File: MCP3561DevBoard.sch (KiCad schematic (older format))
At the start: 51 parts, among them J1 Conn_Coaxial, J2 Conn_Coaxial, J3 Conn_02x03_Counter_Clockwise, J4 Conn_02x03_Counter_Clockwise, J5 Conn_01x04, J6 Conn_02x03_Counter_Clockwise, J7 Conn_01x10_Male, J8 Screw_Terminal_01x02, U3 TLV9051, U4 ADR366, U5 ADP3330-X, U6 ADP3330-X, U7 MCP3561, U8 Teensy4.1

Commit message: fixed power plane so that it contains voltage reference
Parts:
- added TP9: EXT_SYNC, my_library_foot:TestPoint_Keystone_5000-5004_Miniature, symbol Connector:TestPoint
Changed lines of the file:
@@
 Wire Wire Line
 	1350 6800 1900 6800
-Wire Wire Line
-	1900 7150 2300 7150
 Connection ~ 1900 7150
 Wire Wire Line
@@
 Wire Wire Line
 	1350 5150 1150 5150
+$Comp
+L Connector:TestPoint TP9
+U 1 1 604E5F5B
+P 2450 7150
+F 0 "TP9" H 2508 7268 50  0000 L CNN
+F 1 "EXT_SYNC" H 2508 7177 50  0000 L CNN
+F 2 "my_library_foot:TestPoint_Keystone_5000-5004_Miniature" H 2650 7150 50  0001 C CNN
+F 3 "~" H 2650 7150 50  0001 C CNN
+	1    2450 7150
+	1    0    0    -1
+$EndComp
+Wire Wire Line
+	1900 7150 2450 7150
 $EndSCHEMATC

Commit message: updated schematic and backup
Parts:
- R12: value R_US -> 10R
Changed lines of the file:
@@
 P 7150 4500
 F 0 "R12" H 7218 4546 50  0000 L CNN
-F 1 "R_US" H 7218 4455 50  0000 L CNN
+F 1 "10R" H 7218 4455 50  0000 L CNN
 F 2 "Resistor_SMD:R_0805_2012Metric_Pad1.15x1.40mm_HandSolder" V 7190 4490 50  0001 C CNN
 F 3 "~" H 7150 4500 50  0001 C CNN

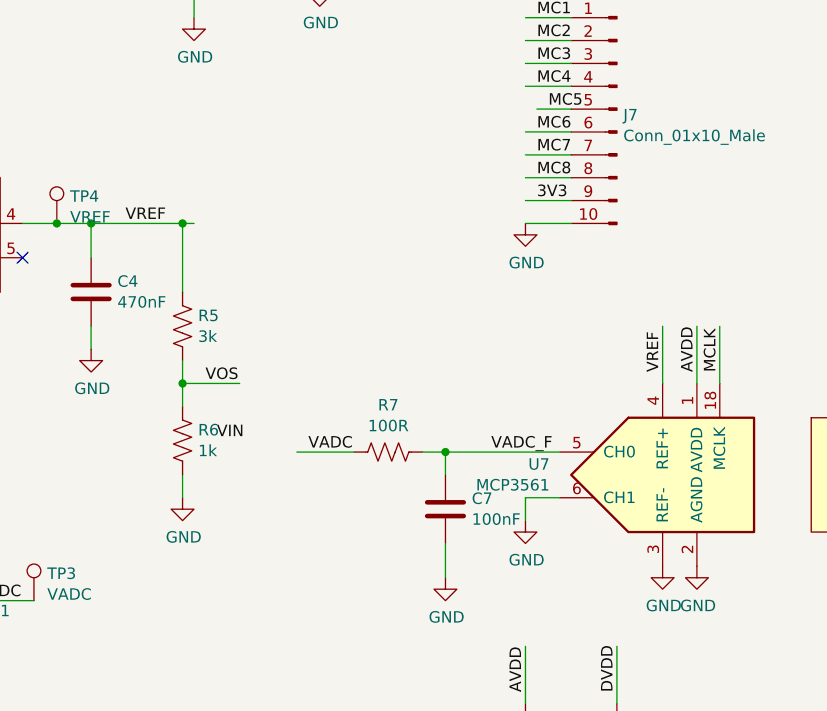
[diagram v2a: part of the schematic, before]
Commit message: added basic arduino code for SCPI communication over serial with arduino. Tested and works at 4.8kHz, there is some funky stuff going on at 38kHz, the ADC has a lower resolution and I'm not sure how to get around that
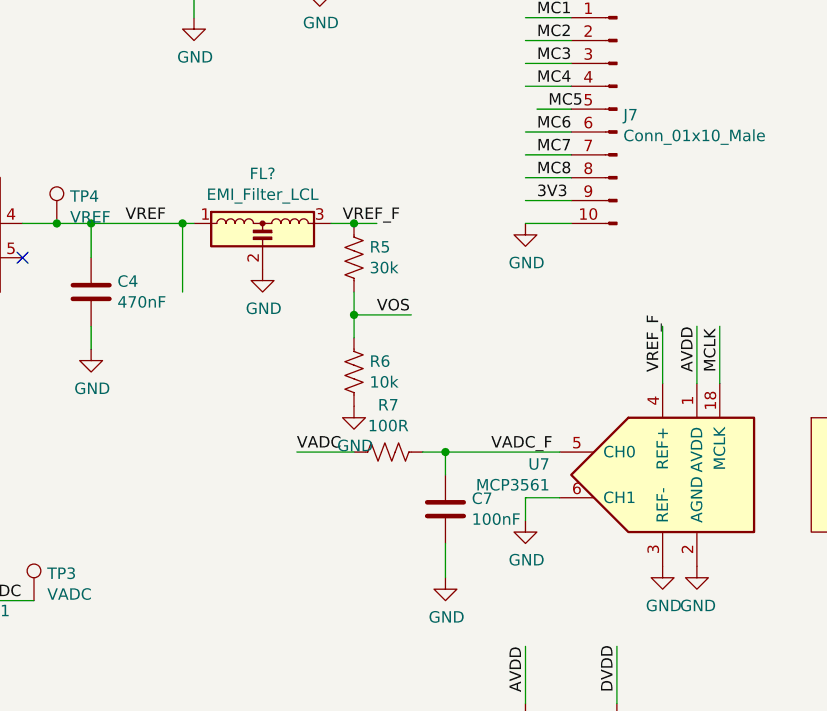
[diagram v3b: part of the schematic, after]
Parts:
- added FL?: EMI_Filter_LCL, my_library_foot:0805_3TERM, symbol Device:EMI_Filter_LCL
- R5: value 3k -> 30k
- R6: value 1k -> 10k
- U3: footprint Package_TO_SOT_SMD:SOT-353_SC-70-5 -> Package_TO_SOT_SMD:SOT-23-5_HandSoldering
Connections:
- net labels added: VREF_F
- wire segments 153 -> 154
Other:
- moved on the sheet: R5, R6
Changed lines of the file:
@@
 Wire Wire Line
 	1100 6300 1100 6150
-Text Label 4200 5150 0    50   ~ 0
-VIN
 $Comp
 L power:GND #PWR029
@@
 	6150 4900 6150 4650
 Text Label 6150 4850 1    50   ~ 0
-VREF
+VREF_F
 Wire Wire Line
 	6400 4900 6400 4650
@@
 F 0 "U3" H 2994 5896 50  0000 L CNN
 F 1 "TLV9051" H 2994 5805 50  0000 L CNN
-F 2 "Package_TO_SOT_SMD:SOT-353_SC-70-5" H 2750 5850 50  0001 C CNN
+F 2 "Package_TO_SOT_SMD:SOT-23-5_HandSoldering" H 2750 5850 50  0001 C CNN
 F 3 "http://www.ti.com/lit/ds/symlink/tlv172.pdf" H 2550 5850 50  0001 C CNN
 	1    2550 5850
@@
 L Device:R_US R5
 U 1 1 600653AE
-P 4050 4650
-F 0 "R5" H 4118 4696 50  0000 L CNN
-F 1 "3k" H 4118 4605 50  0000 L CNN
-F 2 "Resistor_SMD:R_0805_2012Metric_Pad1.15x1.40mm_HandSolder" V 4090 4640 50  0001 C CNN
-F 3 "~" H 4050 4650 50  0001 C CNN
-	1    4050 4650
+P 4800 4350
+F 0 "R5" H 4868 4396 50  0000 L CNN
+F 1 "30k" H 4868 4305 50  0000 L CNN
+F 2 "Resistor_SMD:R_0805_2012Metric_Pad1.15x1.40mm_HandSolder" V 4840 4340 50  0001 C CNN
+F 3 "~" H 4800 4350 50  0001 C CNN
+	1    4800 4350
 	1    0    0    -1
 $EndComp
@@
 L Device:R_US R6
 U 1 1 60065F0A
-P 4050 5150
-F 0 "R6" H 4118 5196 50  0000 L CNN
-F 1 "1k" H 4118 5105 50  0000 L CNN
-F 2 "Resistor_SMD:R_0805_2012Metric_Pad1.15x1.40mm_HandSolder" V 4090 5140 50  0001 C CNN
-F 3 "~" H 4050 5150 50  0001 C CNN
-	1    4050 5150
-	1    0    0    -1
-$EndComp
-Wire Wire Line
-	4050 5000 4050 4900
+P 4800 4850
+F 0 "R6" H 4868 4896 50  0000 L CNN
+F 1 "10k" H 4868 4805 50  0000 L CNN
+F 2 "Resistor_SMD:R_0805_2012Metric_Pad1.15x1.40mm_HandSolder" V 4840 4840 50  0001 C CNN
+F 3 "~" H 4800 4850 50  0001 C CNN
+	1    4800 4850
+	1    0    0    -1
+$EndComp
+Wire Wire Line
+	4800 4700 4800 4600
 $Comp
 L power:GND #PWR018
 U 1 1 60067B1F
-P 4050 5400
-F 0 "#PWR018" H 4050 5150 50  0001 C CNN
-F 1 "GND" H 4055 5227 50  0000 C CNN
-F 2 "" H 4050 5400 50  0001 C CNN
-F 3 "" H 4050 5400 50  0001 C CNN
-	1    4050 5400
-	1    0    0    -1
-$EndComp
-Wire Wire Line
-	4050 5400 4050 5300
+P 4800 5000
+F 0 "#PWR018" H 4800 4750 50  0001 C CNN
+F 1 "GND" H 4805 4827 50  0000 C CNN
+F 2 "" H 4800 5000 50  0001 C CNN
+F 3 "" H 4800 5000 50  0001 C CNN
+	1    4800 5000
+	1    0    0    -1
+$EndComp
 Wire Wire Line
 	1800 5950 1800 6450
@@
 	1900 5750 2350 5750
 Wire Wire Line
-	4050 4900 4300 4900
-Connection ~ 4050 4900
-Wire Wire Line
-	4050 4900 4050 4800
-Text Label 4150 4900 0    50   ~ 0
+	4800 4600 5050 4600
+Connection ~ 4800 4600
+Wire Wire Line
+	4800 4600 4800 4500
+Text Label 4900 4600 0    50   ~ 0
 VOS
 Wire Wire Line
@@
 SCK
 Wire Wire Line
-	7600 2350 7200 2350
-Text Label 7350 2350 0    50   ~ 0
-~IRQ
-Wire Wire Line
 	7600 2450 7200 2450
 Text Label 7350 2450 0    50   ~ 0
@@
 Wire Wire Line
 	4800 5200 4550 5200
-Text Label 4600 5200 0    50   ~ 0
+Text Label 4550 5200 0    50   ~ 0
 VADC
 Text Label 5400 5200 0    50   ~ 0
@@
 Wire Wire Line
 	1900 7150 2450 7150
+$Comp
+L Device:EMI_Filter_LCL FL?
+U 1 1 601181D7
+P 4400 4300
+F 0 "FL?" H 4400 4617 50  0000 C CNN
+F 1 "EMI_Filter_LCL" H 4400 4526 50  0000 C CNN
+F 2 "my_library_foot:0805_3TERM" V 4400 4300 50  0001 C CNN
+F 3 "http://www.murata.com/~/media/webrenewal/support/library/catalog/products/emc/emifil/c31e.ashx?la=en-gb" V 4400 4300 50  0001 C CNN
+	1    4400 4300
+	1    0    0    -1
+$EndComp
+$Comp
+L power:GND #PWR?
+U 1 1 601197C2
+P 4400 4400
+F 0 "#PWR?" H 4400 4150 50  0001 C CNN
+F 1 "GND" H 4405 4227 50  0000 C CNN
+F 2 "" H 4400 4400 50  0001 C CNN
+F 3 "" H 4400 4400 50  0001 C CNN
+	1    4400 4400
+	1    0    0    -1
+$EndComp
+Wire Wire Line
+	4700 4200 4800 4200
+Text Label 4750 4200 0    50   ~ 0
+VREF_F
+Connection ~ 4800 4200
+Wire Wire Line
+	4800 4200 4900 4200
+Text Label 7350 2350 0    50   ~ 0
+~IRQ
+Wire Wire Line
+	7600 2350 7200 2350
 $EndSCHEMATC
